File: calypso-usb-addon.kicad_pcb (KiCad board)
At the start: 2 copper layers, 37.8 x 50.4 mm, 11 parts, among them J1 Conn_02x12_Odd_Even, J2 Conn_02x12_Odd_Even, J3 USB_B_Micro, J4 USB_A_Stacked, J5 USB_A_Stacked, U1 HS8836A

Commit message: psram addition
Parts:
- added R3: 10K, Resistor_SMD:R_1206_3216Metric_Pad1.30x1.75mm_HandSolder, F.Cu at (71.1, 83.8)
- added U2: ESP-PSRAM64H, Package_SO:SOIC-8_3.9x4.9mm_P1.27mm, F.Cu at (78.8, 84.5)
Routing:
- net GND: track 178.0 -> 0.00 mm
- net CYC_AUX0: track 8.06 -> 66.4 mm
- net +3.3VP: track 9.40 -> 43.1 mm, vias 0 -> 1
- net CYC_AUX1: track 8.06 -> 35.7 mm
- net CYC_AUX3: track 8.06 -> 26.3 mm, vias 0 -> 1
- net CYC_AUX2: track 8.06 -> 24.6 mm, vias 0 -> 1
- net CYC_AUX4: track 8.05 -> 22.9 mm
- net DM2: track 31.1 -> 44.9 mm, vias 0 -> 1
- net DP2: track 33.2 -> 46.1 mm
- net CYC_AUX5: track 8.06 -> 20.6 mm
- net +5V: track 69.1 -> 74.7 mm
- net Net-(U1-VCC): track 23.2 -> 27.2 mm
- net UP: track 39.7 -> 37.1 mm, vias 0 -> 2
- net DP1: track 26.4 -> 27.6 mm
- net DM1: track 27.6 -> 26.9 mm
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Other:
- board text added: "Calypso USB Add-On v0.2"
- board text removed: "Calypso USB Add-On v0.1"

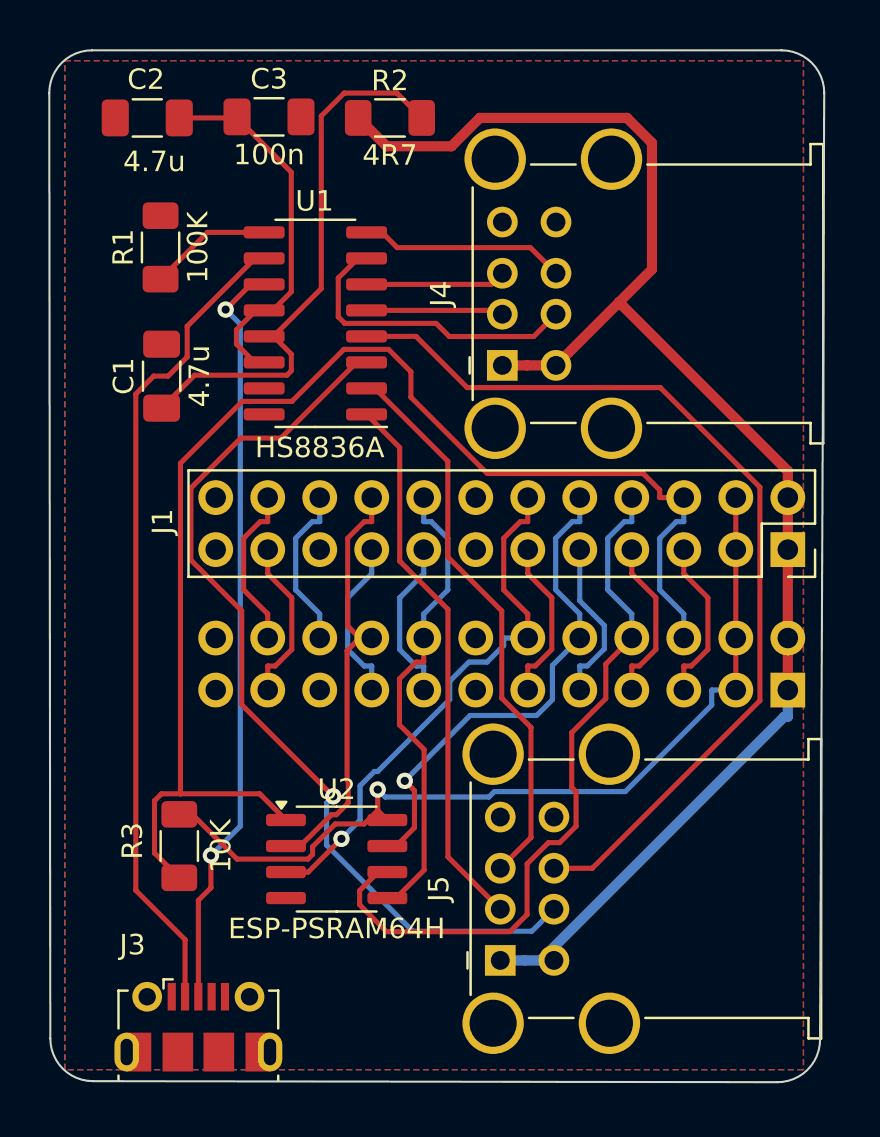
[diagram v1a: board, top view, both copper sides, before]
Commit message: Fix connector lines
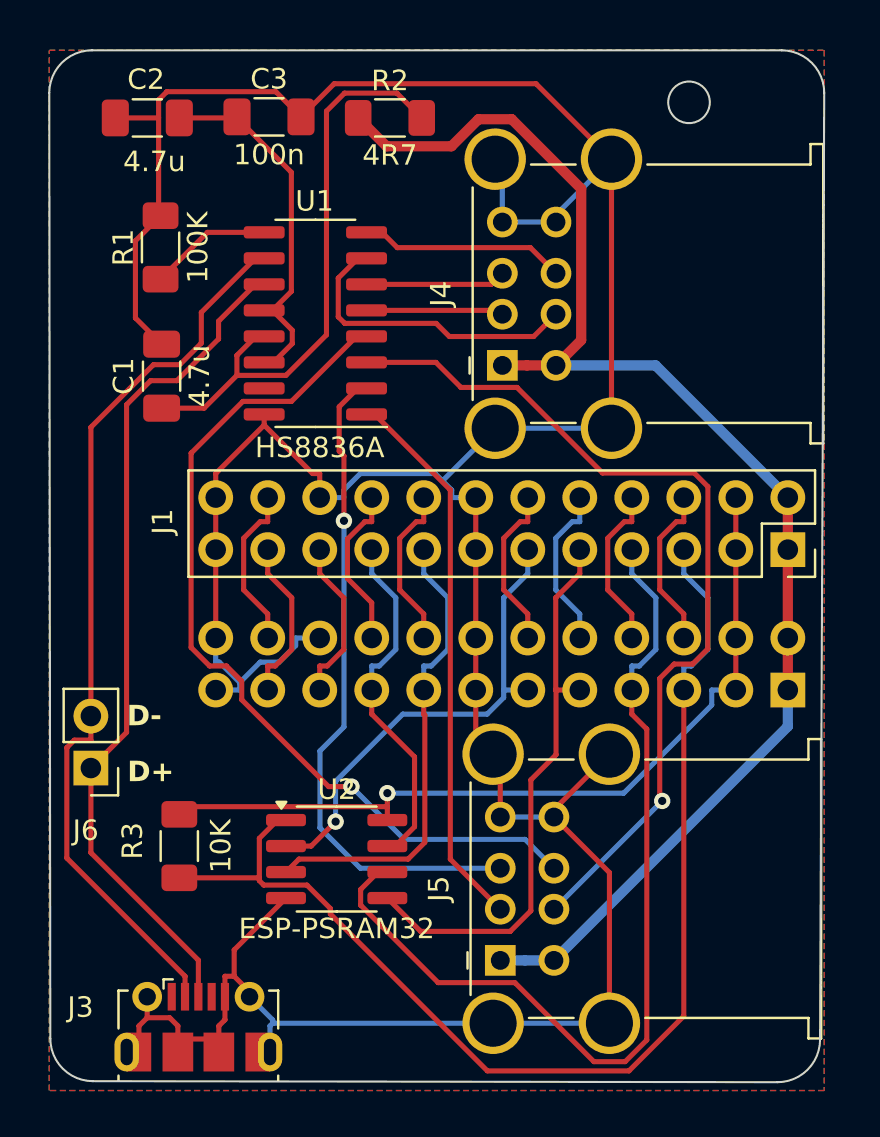
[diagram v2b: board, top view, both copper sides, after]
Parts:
- added J6: Conn_01x02_Pin, Connector_PinHeader_2.54mm:PinHeader_1x02_P2.54mm_Vertical, F.Cu at (66.8, 80.0)
- U2: value ESP-PSRAM64H -> ESP-PSRAM32
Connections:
- J1 pad 10: CYC_AUX2 -> RP_AUX2
- J1 pad 11: RP_AUX3 -> CYC_AUX3
- J1 pad 12: CYC_AUX3 -> RP_AUX3
- J1 pad 15: SER_RX -> CYC_AUX4
- J1 pad 16: CYC_AUX4 -> SER_RX
- J1 pad 17: SER_TX -> CYC_AUX5
- J1 pad 18: CYC_AUX5 -> SER_TX
- J1 pad 19: GND -> CYC_AUX6
- J1 pad 20: CYC_AUX6 -> GND
- J1 pad 21: RP_RESET -> CYC_AUX7
- J1 pad 22: CYC_AUX7 -> RP_RESET
- J1 pad 5: RP_AUX0 -> CYC_AUX0
- J1 pad 6: CYC_AUX0 -> RP_AUX0
- J1 pad 7: RP_AUX1 -> CYC_AUX1
- J1 pad 8: CYC_AUX1 -> RP_AUX1
- J1 pad 9: RP_AUX2 -> CYC_AUX2
- J2 pad 10: CYC_AUX2 -> RP_AUX2
- J2 pad 11: RP_AUX3 -> CYC_AUX3
- J2 pad 12: CYC_AUX3 -> RP_AUX3
- J2 pad 15: SER_RX -> CYC_AUX4
- J2 pad 16: CYC_AUX4 -> SER_RX
- J2 pad 17: SER_TX -> CYC_AUX5
- J2 pad 18: CYC_AUX5 -> SER_TX
- J2 pad 19: GND -> CYC_AUX6
- J2 pad 20: CYC_AUX6 -> GND
- J2 pad 21: RP_RESET -> CYC_AUX7
- J2 pad 22: CYC_AUX7 -> RP_RESET
- J2 pad 5: RP_AUX0 -> CYC_AUX0
- J2 pad 6: CYC_AUX0 -> RP_AUX0
- J2 pad 7: RP_AUX1 -> CYC_AUX1
- J2 pad 8: CYC_AUX1 -> RP_AUX1
- J2 pad 9: RP_AUX2 -> CYC_AUX2
- U2 pad 2: CYC_AUX5 -> CYC_AUX3
- U2 pad 3: CYC_AUX3 -> CYC_AUX4
- U2 pad 5: CYC_AUX4 -> CYC_AUX2
- U2 pad 7: CYC_AUX2 -> CYC_AUX5
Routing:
- net GND: track 0.00 -> 181.2 mm
- net CYC_AUX1: track 35.7 -> 45.4 mm
- net CYC_AUX0: track 66.4 -> 57.5 mm
- net +5V: track 74.7 -> 69.1 mm
- net DP1: track 27.6 -> 32.5 mm, vias 0 -> 1
- net UP: track 37.1 -> 41.5 mm, vias 2 -> 0
- net UM: track 40.3 -> 43.9 mm
- net CYC_AUX5: track 20.6 -> 17.3 mm
- net CYC_AUX2: track 24.6 -> 27.9 mm, vias 1 -> 0
- net DP2: track 46.1 -> 43.1 mm, vias 0 -> 1
- net CYC_AUX3: track 26.3 -> 23.7 mm
- net +3.3VP: track 43.1 -> 40.6 mm
- net Net-(U1-VCC): track 27.2 -> 28.7 mm
- net DM2: track 44.9 -> 43.6 mm
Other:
- outline, holes or cut-outs redrawn
- board text added: "Calypso PowerPack v0.1"
- board text added: "D+"
- board text added: "D-"
- board text removed: "Calypso USB Add-On v0.2"
